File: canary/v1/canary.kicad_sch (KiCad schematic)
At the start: 52 parts, among them J1 USB-C power, J2 ISP (Tag-Connect), J3 Probe, Q1 AO3400A, SW1 TEST / HUSH, U1 AP2112K-3.3, U2 ATmega328P-AU, U3 SGP40, U4 SHT40, U5 SCD41

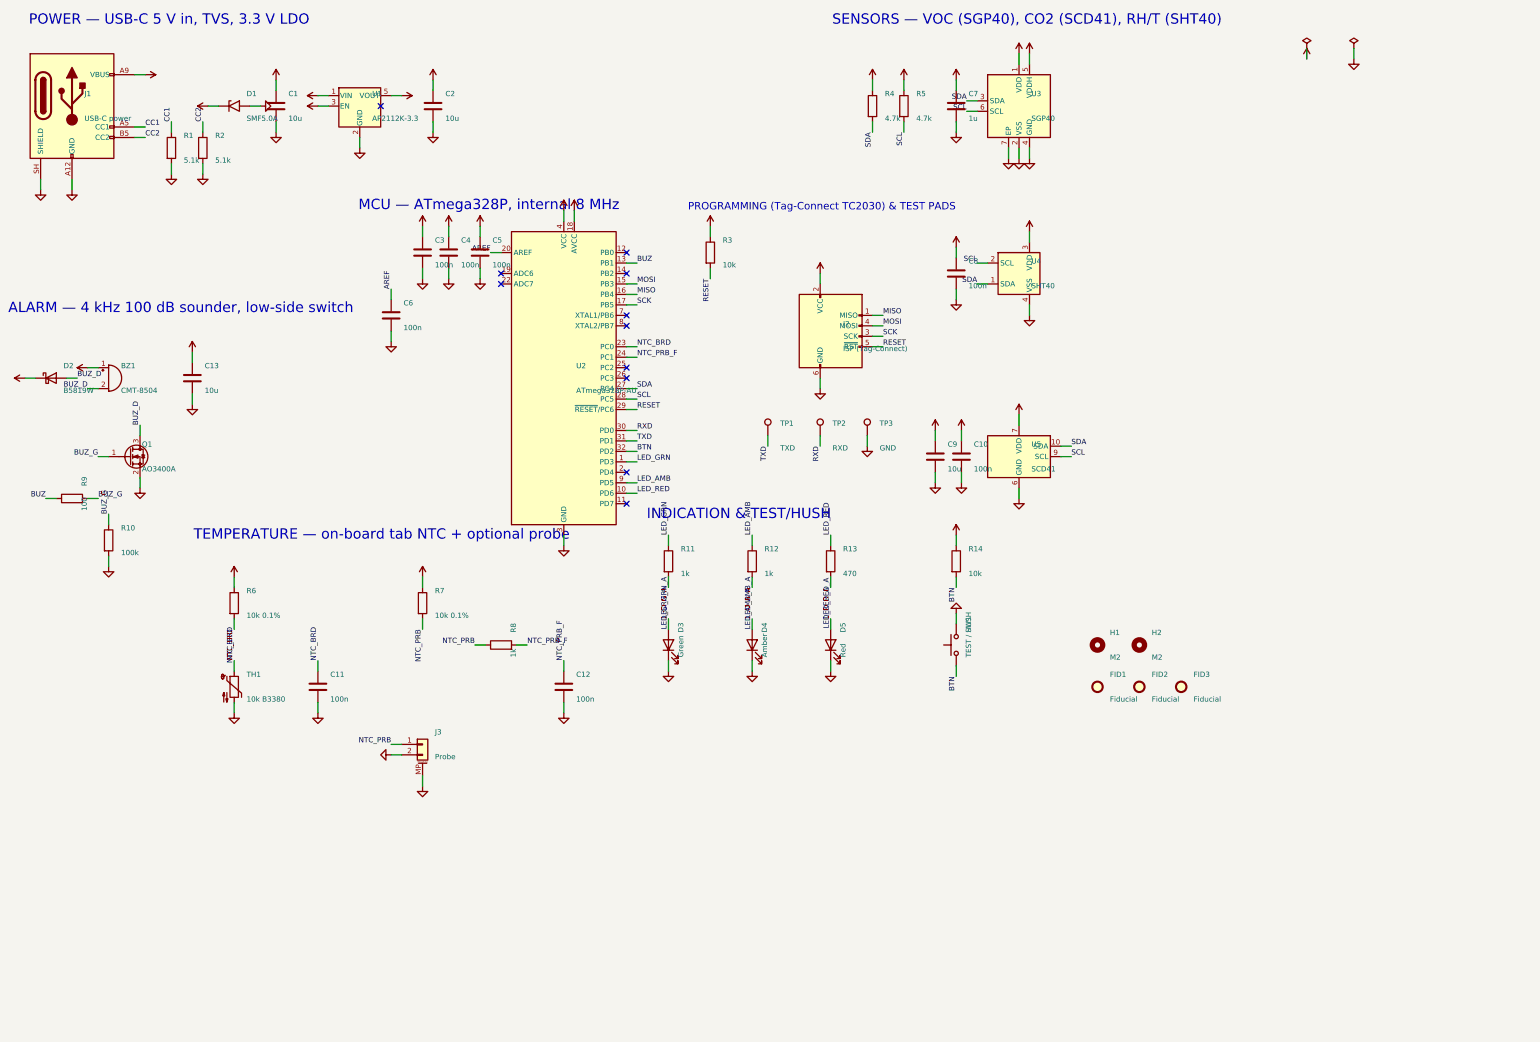
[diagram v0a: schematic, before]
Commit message: Canary v1: readable schematic layout (same netlist)
Co-Authored-By: Claude Opus 5.5 <noreply@anthropic.com>
Claude-Session: https://claude.ai/code/session_01YFfBHwLKmoNTwrpibShML1
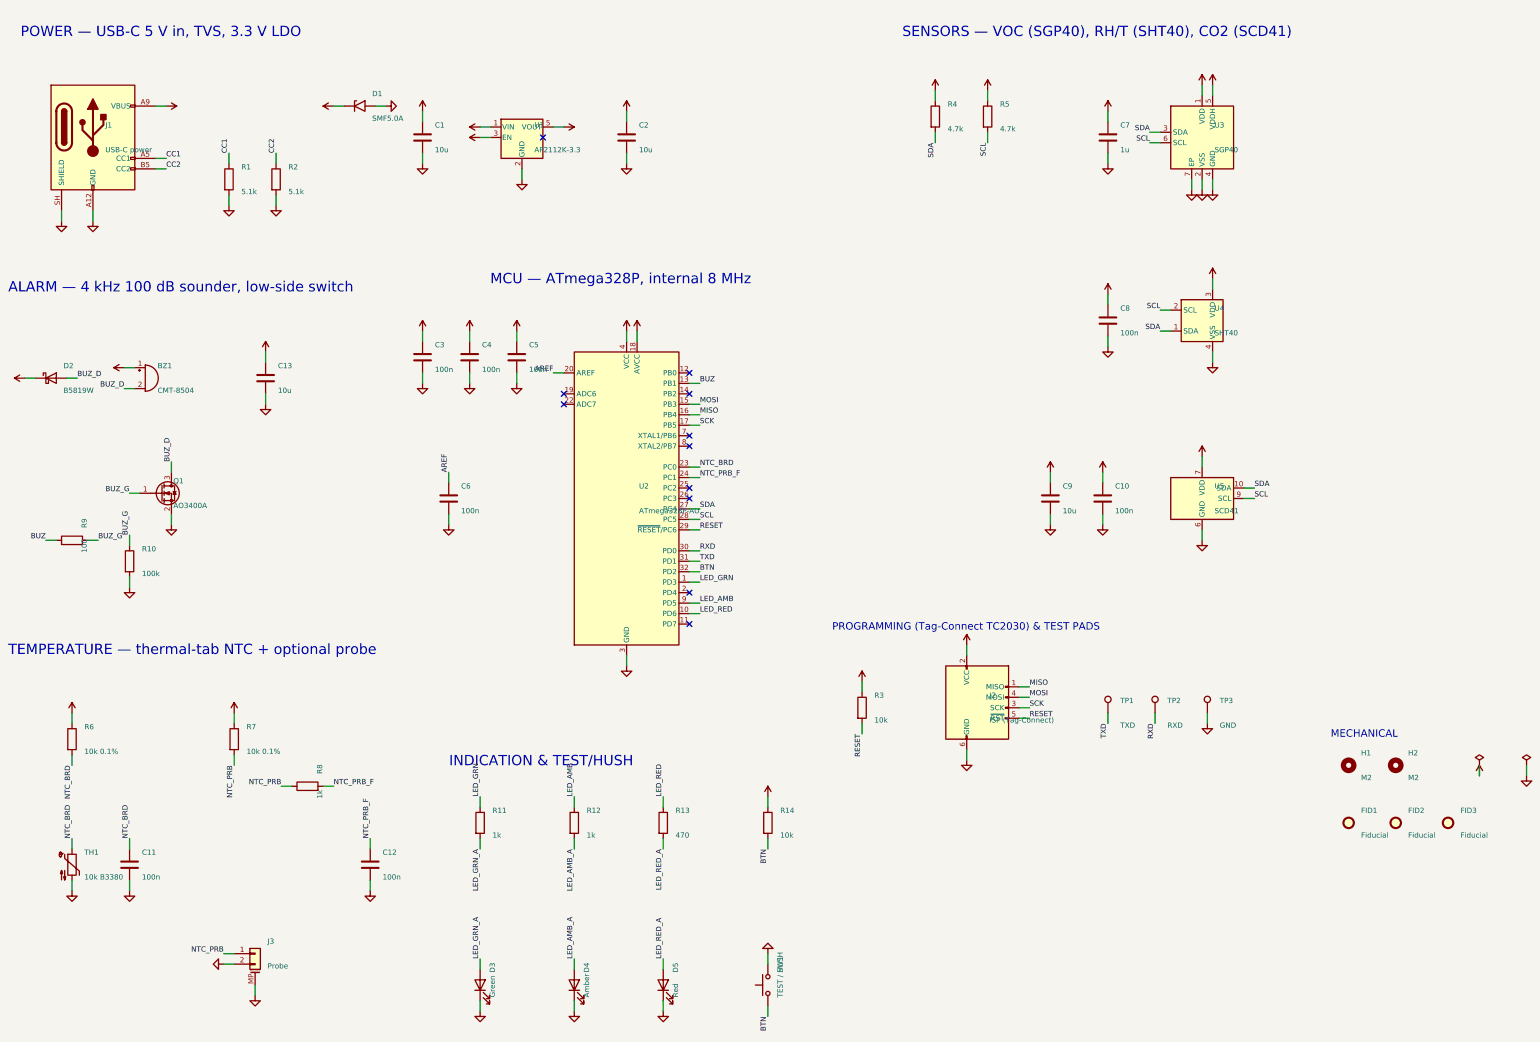
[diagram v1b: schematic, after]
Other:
- note added: "MECHANICAL"
- note added: "SENSORS — VOC (SGP40), RH/T (SHT40), CO2 (SCD41)"
- note added: "TEMPERATURE — thermal-tab NTC + optional probe"
- note removed: "SENSORS — VOC (SGP40), CO2 (SCD41), RH/T (SHT40)"
- note removed: "TEMPERATURE — on-board tab NTC + optional probe"
- moved on the sheet: BZ1, C1, C10, C11, C12, C13, C2, C3, C4, C5, C6, C7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
